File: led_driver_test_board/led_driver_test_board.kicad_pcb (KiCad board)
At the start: 2 copper layers, 49 parts, among them Q1 Q_NMOS_SSM3K09FULF, Q2 Q_NMOS_SSM3K09FULF, Q3 Q_NMOS_SSM3K09FULF, Q4 Q_NMOS_SSM3K09FULF, Q5 Q_NMOS_SSM3K09FULF, Q6 Q_NMOS_SSM3K09FULF, U1 connex_EFM32ZG222F16-QFP48

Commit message: Initial routing
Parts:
- moved D1 131.7 mm to (118.1, 95.2)
- moved D2 127.5 mm to (121.2, 95.2)
- moved R16 126.4 mm to (123.8, 111.8), turned to 270 degrees
- moved Q1 121.4 mm to (123.8, 105.8)
- moved Q2 115.4 mm to (129.8, 105.8)
- moved R3 113.3 mm to (115.2, 103.2), turned to 180 degrees
- moved D3 111.5 mm to (124.2, 95.2)
- moved Q5 111.4 mm to (129.8, 115.2)
- moved R12 110.0 mm to (137.8, 102.2), turned to 270 degrees
- moved D8 110.0 mm to (139.2, 95.2)
- moved D5 103.5 mm to (130.2, 95.2)
- moved Q4 102.8 mm to (123.8, 115.2)
- moved R18 100.3 mm to (127.8, 111.8), turned to 270 degrees
- moved R7 98.8 mm to (127.8, 102.2), turned to 270 degrees
- moved D6 98.3 mm to (133.2, 95.2)
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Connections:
- U1 pad 13: /LED_SEL4 -> /LED1
- U1 pad 14: /LED_SEL5 -> /LED2
- U1 pad 15: /LED_SEL6 -> /LED3
- U1 pad 17: /LED_SEL7 -> /LED4
- U1 pad 30: /LED_SEL0 -> /LED8
- U1 pad 31: /LED_SEL1 -> /LED7
- U1 pad 32: /LED_SEL2 -> /LED6
- U1 pad 33: /LED_SEL3 -> /LED5
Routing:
- net GND: track 0.00 -> 60.5 mm, vias 0 -> 18
- net /LED8: track 0.00 -> 56.2 mm, vias 0 -> 2
- net /LED7: track 0.00 -> 52.4 mm, vias 0 -> 2
- net /LED6: track 0.00 -> 48.4 mm, vias 0 -> 2
- net /LED4: track 0.00 -> 47.1 mm, vias 0 -> 2
- net /LED3: track 0.00 -> 45.9 mm, vias 0 -> 2
- net /LED2: track 0.00 -> 44.9 mm, vias 0 -> 2
- net /LED1: track 0.00 -> 44.5 mm, vias 0 -> 2
- net /LED5: track 0.00 -> 44.4 mm, vias 0 -> 2
- net /LED_DRV_RED: track 0.00 -> 42.4 mm
- net /LED_DRV_BLUE: track 0.00 -> 39.3 mm
- net Net-(C4-Pad1): track 0.00 -> 36.9 mm, vias 0 -> 2
- net /LED_GREEN: track 0.00 -> 36.5 mm
- net /PWM_RED1: track 0.00 -> 35.9 mm
- net /LED_RED: track 0.00 -> 34.5 mm
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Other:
- net class Default: trace_width 0.25 -> 0.2

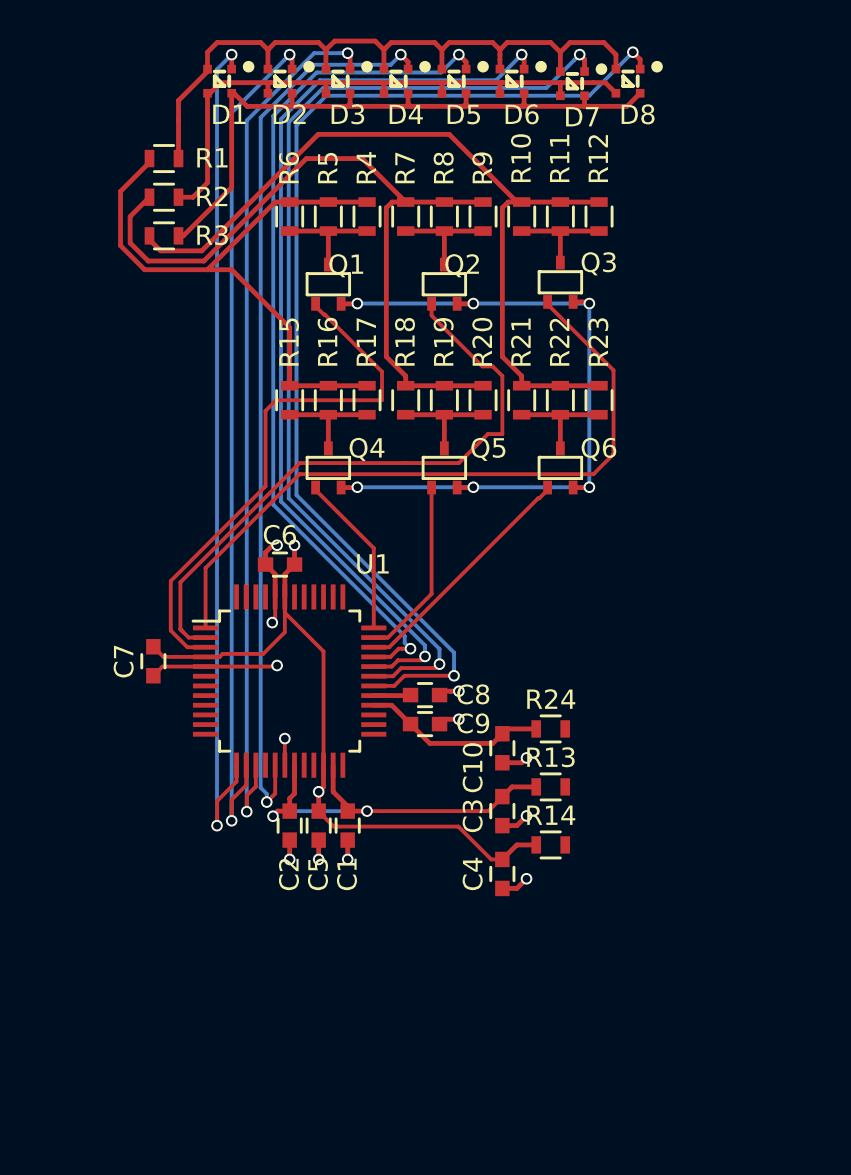
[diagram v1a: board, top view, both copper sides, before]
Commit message: Added crystal and some changes to connector pinout. Continued routing pcb
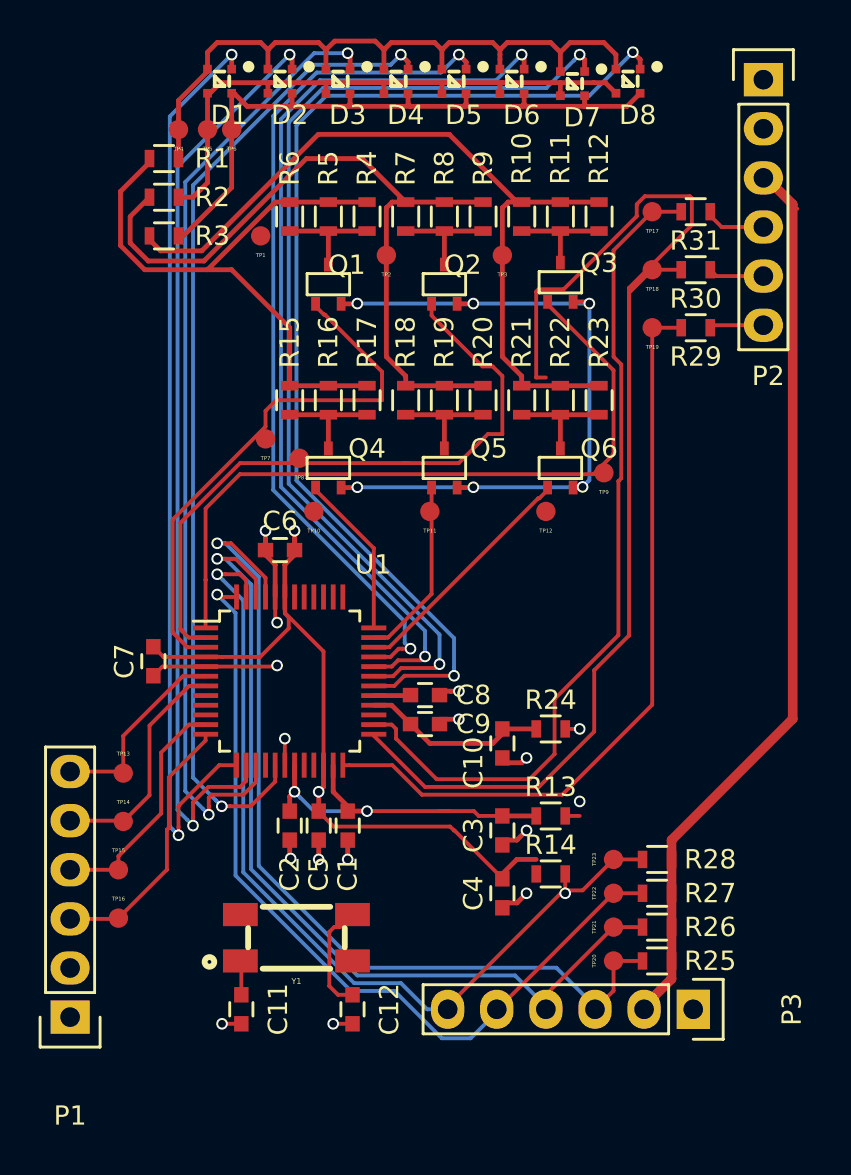
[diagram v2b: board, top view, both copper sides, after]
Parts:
- added C11: connex_cap_30PF_0603_50V, Capacitors_SMD:C_0603, F.Cu at (119.2, 143.2)
- added C12: connex_cap_30PF_0603_50V, Capacitors_SMD:C_0603, F.Cu at (125.0, 143.2)
- added P1: CONN_01X06_M50-3530642, Pin_Headers:Pin_Header_Straight_1x06, F.Cu at (110.4, 143.7)
- added P2: CONN_01X06_M50-3530642, Pin_Headers:Pin_Header_Straight_1x06, F.Cu at (146.2, 95.2)
- added P3: CONN_01X06_M50-3530642, Pin_Headers:Pin_Header_Straight_1x06, F.Cu at (142.6, 143.2)
- added R25: SMD-RES-10K-1%-1_10W_0603_, Resistors_SMD:R_0603, F.Cu at (140.8, 140.8)
- added R26: SMD-RES-10K-1%-1_10W_0603_, Resistors_SMD:R_0603, F.Cu at (140.8, 139.0)
- added R27: SMD-RES-10K-1%-1_10W_0603_, Resistors_SMD:R_0603, F.Cu at (140.8, 137.2)
- added R28: SMD-RES-10K-1%-1_10W_0603_, Resistors_SMD:R_0603, F.Cu at (140.8, 135.5)
- added R29: SMD-RES-0R-1_4W_0603_, Resistors_SMD:R_0603, F.Cu at (142.8, 108.0)
- added R30: SMD-RES-0R-1_4W_0603_, Resistors_SMD:R_0603, F.Cu at (142.8, 105.0)
- added R31: SMD-RES-0R-1_4W_0603_, Resistors_SMD:R_0603, F.Cu at (142.8, 102.0)
- added TP1: test_point_smt, connex_test:TEST_POINT_SMD_50MIL, F.Cu at (120.2, 103.2)
- added TP10: test_point_smt, connex_test:TEST_POINT_SMD_50MIL, F.Cu at (123.0, 117.5)
- added TP11: test_point_smt, connex_test:TEST_POINT_SMD_50MIL, F.Cu at (129.0, 117.5)
- added TP12: test_point_smt, connex_test:TEST_POINT_SMD_50MIL, F.Cu at (135.0, 117.5)
- added TP13: test_point_smt, connex_test:TEST_POINT_SMD_50MIL, F.Cu at (113.1, 131.0)
- added TP14: test_point_smt, connex_test:TEST_POINT_SMD_50MIL, F.Cu at (113.1, 133.5)
- added TP15: test_point_smt, connex_test:TEST_POINT_SMD_50MIL, F.Cu at (112.9, 136.0)
- added TP16: test_point_smt, connex_test:TEST_POINT_SMD_50MIL, F.Cu at (112.9, 138.5)
- added TP17: test_point_smt, connex_test:TEST_POINT_SMD_50MIL, F.Cu at (140.5, 102.0)
- added TP18: test_point_smt, connex_test:TEST_POINT_SMD_50MIL, F.Cu at (140.5, 105.0)
- added TP19: test_point_smt, connex_test:TEST_POINT_SMD_50MIL, F.Cu at (140.5, 108.0)
- added TP2: test_point_smt, connex_test:TEST_POINT_SMD_50MIL, F.Cu at (126.8, 104.2)
- added TP20: test_point_smt, connex_test:TEST_POINT_SMD_50MIL, F.Cu at (138.5, 140.8)
- added TP21: test_point_smt, connex_test:TEST_POINT_SMD_50MIL, F.Cu at (138.5, 139.0)
- added TP22: test_point_smt, connex_test:TEST_POINT_SMD_50MIL, F.Cu at (138.5, 137.2)
- added TP23: test_point_smt, connex_test:TEST_POINT_SMD_50MIL, F.Cu at (138.5, 135.5)
- added TP3: test_point_smt, connex_test:TEST_POINT_SMD_50MIL, F.Cu at (132.8, 104.2)
- added TP4: test_point_smt, connex_test:TEST_POINT_SMD_50MIL, F.Cu at (116.0, 97.8)
- added TP5: test_point_smt, connex_test:TEST_POINT_SMD_50MIL, F.Cu at (117.5, 97.8)
- added TP6: test_point_smt, connex_test:TEST_POINT_SMD_50MIL, F.Cu at (118.8, 97.8)
- added TP7: test_point_smt, connex_test:TEST_POINT_SMD_50MIL, F.Cu at (120.5, 113.8)
- added TP8: test_point_smt, connex_test:TEST_POINT_SMD_50MIL, F.Cu at (122.2, 114.8)
- added TP9: test_point_smt, connex_test:TEST_POINT_SMD_50MIL, F.Cu at (138.0, 115.5)
- added Y1: Crystal_8MHZ_ABM3B-8.000MHZ-B2-T, connex_crystal:CONNEX_CRYSTAL_4SMD_32X50, F.Cu at (122.1, 139.6)
- moved R13 1.50 mm to (135.2, 133.2)
- moved R14 1.50 mm to (135.2, 136.2)
- moved C3 1.00 mm to (132.8, 134.0)
- moved C4 1.00 mm to (132.8, 137.2)
- moved C6 0.75 mm to (121.2, 119.5)
- moved C10 0.25 mm to (132.8, 129.5)
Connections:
- U1 pad 10: /FRAME_SYNC -> Net-(U1-Pad10)
- U1 pad 26: /I2C0_SDA -> /FRAME_SYNC
- U1 pad 27: /I2C0_SCL -> Net-(U1-Pad27)
- U1 pad 45: Net-(U1-Pad45) -> /I2C0_INT1
- U1 pad 46: Net-(U1-Pad46) -> /I2C0_INT2
- U1 pad 47: Net-(U1-Pad47) -> /I2C0_SDA
- U1 pad 48: Net-(U1-Pad48) -> /I2C0_SCL
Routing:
- net /EXTRA_ADC: track 0.00 -> 71.8 mm
- net +3V3: track 0.00 -> 57.9 mm, vias 0 -> 2
- net /I2C0_INT1: track 0.00 -> 47.0 mm, vias 0 -> 1
- net /I2C0_INT2: track 0.00 -> 45.9 mm, vias 0 -> 1
- net /I2C0_SDA: track 0.00 -> 44.4 mm, vias 0 -> 1
- net /I2C0_SCL: track 0.00 -> 43.7 mm, vias 0 -> 1
- net /FRAME_SYNC: track 0.00 -> 43.3 mm
- net /BATTERY_ADC: track 0.00 -> 39.6 mm
- net /SPI_CS: track 0.00 -> 13.9 mm
- net /SPI_SIMO: track 0.00 -> 12.4 mm
- net /SPI_CLK: track 0.00 -> 12.4 mm
- net /SPI_MOSI: track 0.00 -> 10.2 mm
- net Net-(C12-Pad1): track 0.00 -> 5.76 mm
- net /LED4: track 47.1 -> 51.3 mm
- net /LED3: track 45.9 -> 49.8 mm
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
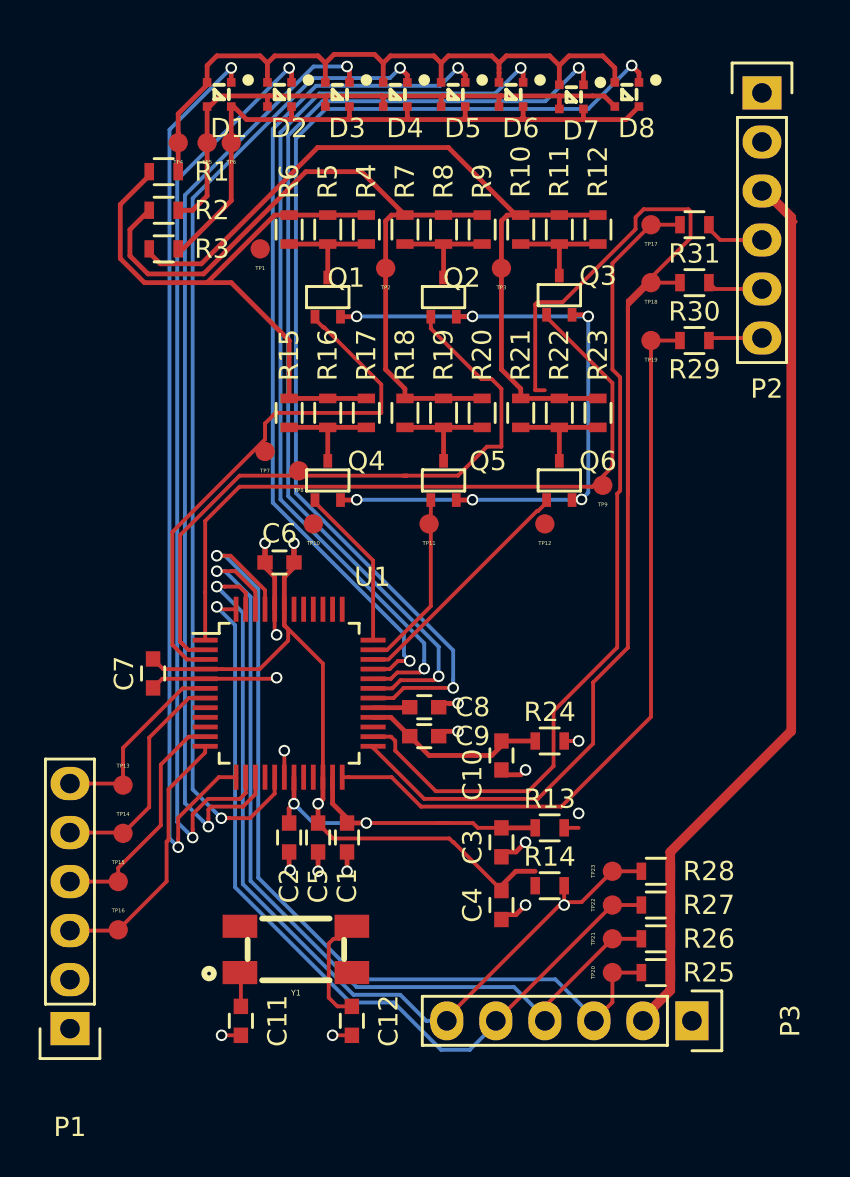
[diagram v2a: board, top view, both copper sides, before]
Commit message: Added regulator to schematic. Routed regulator on board. Adjusted headers
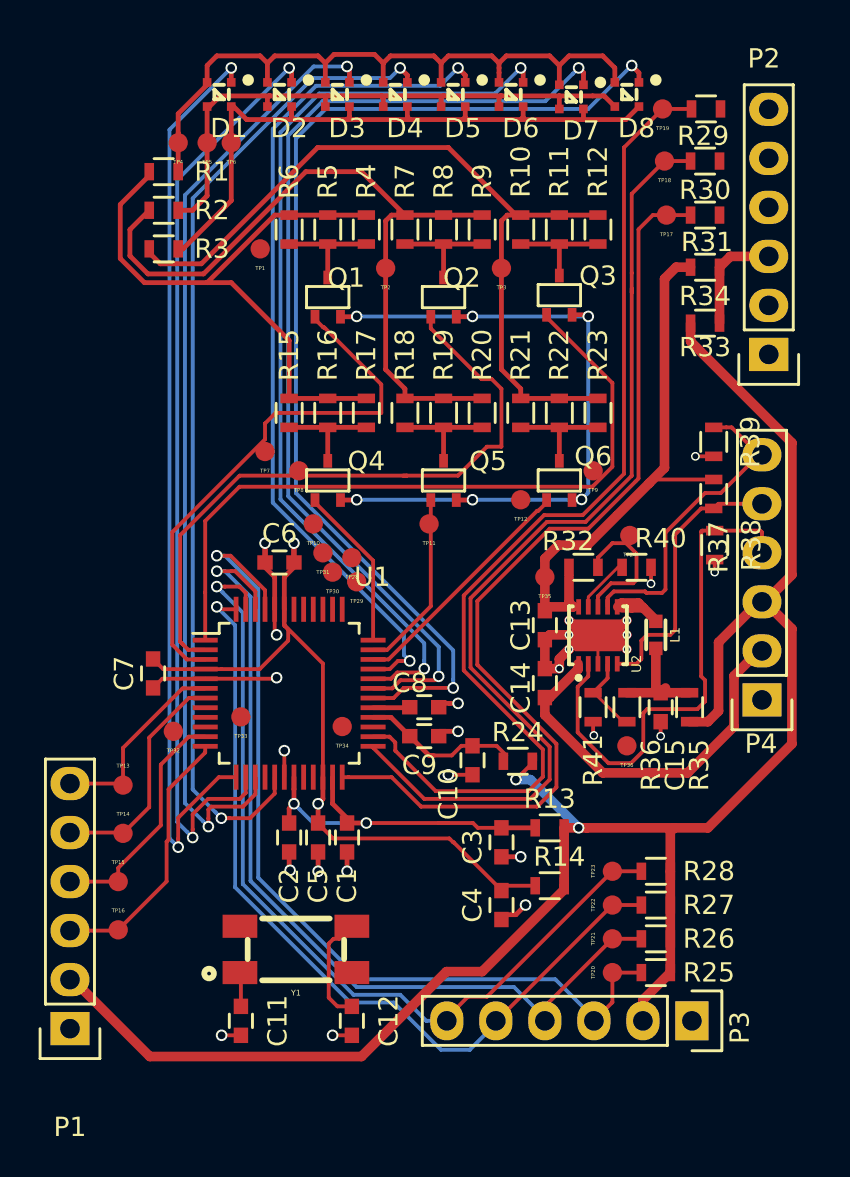
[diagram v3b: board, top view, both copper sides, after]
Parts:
- added C13: CONNEX-SMD-CAP-4700NF-0603, Capacitors_SMD:C_0603, F.Cu at (135.0, 122.8)
- added C14: CONNEX-SMD-CAP-4700NF-0603, Capacitors_SMD:C_0603, F.Cu at (135.0, 125.8)
- added C15: CONNEX-SMD-CAP-4700NF-0603, Capacitors_SMD:C_0603, F.Cu at (141.0, 127.0)
- added L1: CONNEX-SMD-INDUCTOR-6R8M-0603, connex_inductor:L_0603, F.Cu at (140.8, 123.2)
- added P4: CONN_01X06_M50-3530642, Pin_Headers:Pin_Header_Straight_1x06, F.Cu at (146.2, 126.6)
- added R32: SMD-RES-10K-1%-1_10W_0603_, Resistors_SMD:R_0603, F.Cu at (137.0, 119.8)
- added R33: SMD-RES-0R-1_4W_0603_, Resistors_SMD:R_0603, F.Cu at (143.3, 107.1)
- added R34: SMD-RES-0R-1_4W_0603_, Resistors_SMD:R_0603, F.Cu at (143.3, 104.2)
- added R35: CONNEX-SMD-RES-0-0603, Resistors_SMD:R_0603, F.Cu at (142.5, 127.0)
- added R36: CONNEX-SMD-RES-1M-0603, Resistors_SMD:R_0603, F.Cu at (139.2, 127.0)
- added R37: SMD-RES-10K-1%-1_10W_0603_, Resistors_SMD:R_0603, F.Cu at (143.8, 116.0)
- added R38: SMD-RES-10K-1%-1_10W_0603_, Resistors_SMD:R_0603, F.Cu at (143.8, 118.6)
- added R39: SMD-RES-10K-1%-1_10W_0603_, Resistors_SMD:R_0603, F.Cu at (143.8, 113.2)
- added R40: CONNEX-SMD-RES-0-0603, Resistors_SMD:R_0603, F.Cu at (139.8, 119.8)
- added R41: CONNEX-SMD-RES-324K-0603, Resistors_SMD:R_0603, F.Cu at (137.5, 127.0)
- added TP24: test_point_smt, connex_test:TEST_POINT_SMD_50MIL, F.Cu at (139.4, 118.1)
- added TP28: test_point_smt, connex_test:TEST_POINT_SMD_50MIL, F.Cu at (125.0, 119.2)
- added TP29: test_point_smt, connex_test:TEST_POINT_SMD_50MIL, F.Cu at (125.2, 120.5)
- added TP30: test_point_smt, connex_test:TEST_POINT_SMD_50MIL, F.Cu at (124.0, 120.0)
- added TP31: test_point_smt, connex_test:TEST_POINT_SMD_50MIL, F.Cu at (123.5, 119.0)
- added TP32: test_point_smt, connex_test:TEST_POINT_SMD_50MIL, F.Cu at (115.8, 128.2)
- added TP33: test_point_smt, connex_test:TEST_POINT_SMD_50MIL, F.Cu at (119.2, 127.5)
- added TP34: test_point_smt, connex_test:TEST_POINT_SMD_50MIL, F.Cu at (124.5, 128.0)
- added TP35: test_point_smt, connex_test:TEST_POINT_SMD_50MIL, F.Cu at (135.0, 120.2)
- added TP36: test_point_smt, connex_test:TEST_POINT_SMD_50MIL, F.Cu at (139.2, 129.0)
- added U2: CONNEX_REGUL_LT4081, connex_smd_misc:CONNEX_DFN_10PIN_3MMX3MM, F.Cu at (137.8, 123.3)
- moved P2 13.6 mm to (146.6, 108.7), turned to 180 degrees
- moved R29 12.0 mm to (143.3, 96.0)
- moved TP19 12.0 mm to (141.1, 96.0)
- moved TP18 6.34 mm to (141.2, 98.7)
- moved R30 6.32 mm to (143.3, 98.7)
- moved R24 1.96 mm to (133.6, 129.8)
- moved TP12 1.77 mm to (133.8, 116.2)
- moved C10 1.52 mm to (131.2, 129.8)
- moved TP17 0.94 mm to (141.3, 101.5)
- moved TP9 0.90 mm to (137.5, 114.8)
- moved R31 0.74 mm to (143.3, 101.5)
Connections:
- P2 pad 3: +3V3 -> /POWER_INPUT_CONN
- P2 pad 4: /EXTRA_GPIO_CONN -> /BATTERY_ADC_CONN
- P2 pad 6: /BATTERY_ADC_CONN -> /EXTRA_GPIO_CONN
- R29 pad 1: /BATTERY_ADC -> /FRAME_SYNC
- R29 pad 2: /BATTERY_ADC_CONN -> /EXTRA_GPIO_CONN
- R31 pad 1: /FRAME_SYNC -> /BATTERY_ADC
- R31 pad 2: /EXTRA_GPIO_CONN -> /BATTERY_ADC_CONN
- TP17 pad 1: /FRAME_SYNC -> /BATTERY_ADC
- TP19 pad 1: /BATTERY_ADC -> /FRAME_SYNC
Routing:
- net +3V3: track 57.9 -> 98.1 mm
- net /3V3_CHARGE_INPUT: track 0.00 -> 29.0 mm
- net /EN_CHRG: track 0.00 -> 27.4 mm
- net /EXTRA_ADC: track 71.8 -> 51.4 mm
- net /BATT_CONN_OUTPUT: track 0.00 -> 20.2 mm
- net GND: track 63.1 -> 82.8 mm, vias 20 -> 32
- net /MODE: track 0.00 -> 16.5 mm
- net /EN_BUCK: track 0.00 -> 14.4 mm
- net /BATTERY_ADC: track 39.6 -> 50.4 mm
- net /FRAME_SYNC: track 43.3 -> 53.8 mm
- net Net-(R32-Pad1): track 0.00 -> 7.30 mm
- net /POWER_INPUT_CONN: track 0.00 -> 5.68 mm
- net /REG_OUTPUT_3V3: track 0.00 -> 5.65 mm
- net Net-(R36-Pad1): track 0.00 -> 4.18 mm
- net Net-(L1-Pad1): track 0.00 -> 3.60 mm
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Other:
- net class Default: clearance 0.2 -> 0.152; trace_width 0.2 -> 0.152; via_dia 0.6 -> 0.452; via_drill 0.4 -> 0.3
- rule trace_clearance: 0.2 -> 0.152
- rule trace_min: 0.2 -> 0.152
- rule via_min_size: 0.4 -> 0.452
